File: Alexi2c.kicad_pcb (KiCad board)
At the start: 2 copper layers, 50 x 100 mm, 334 parts, among them J1 Conn_01x04, J10 Conn_01x01, J11 Conn_01x09, J12 Conn_01x02, J13 Conn_01x02, J2 Conn_02x03_Odd_Even, J3 Conn_01x02, J4 Conn_01x10, J5 Conn_01x10, J6 Conn_01x09, J8 Conn_01x01, J9 Conn_01x01, U2 TCA9555PWR, U3 ULN2803A, U4 ULN2803A

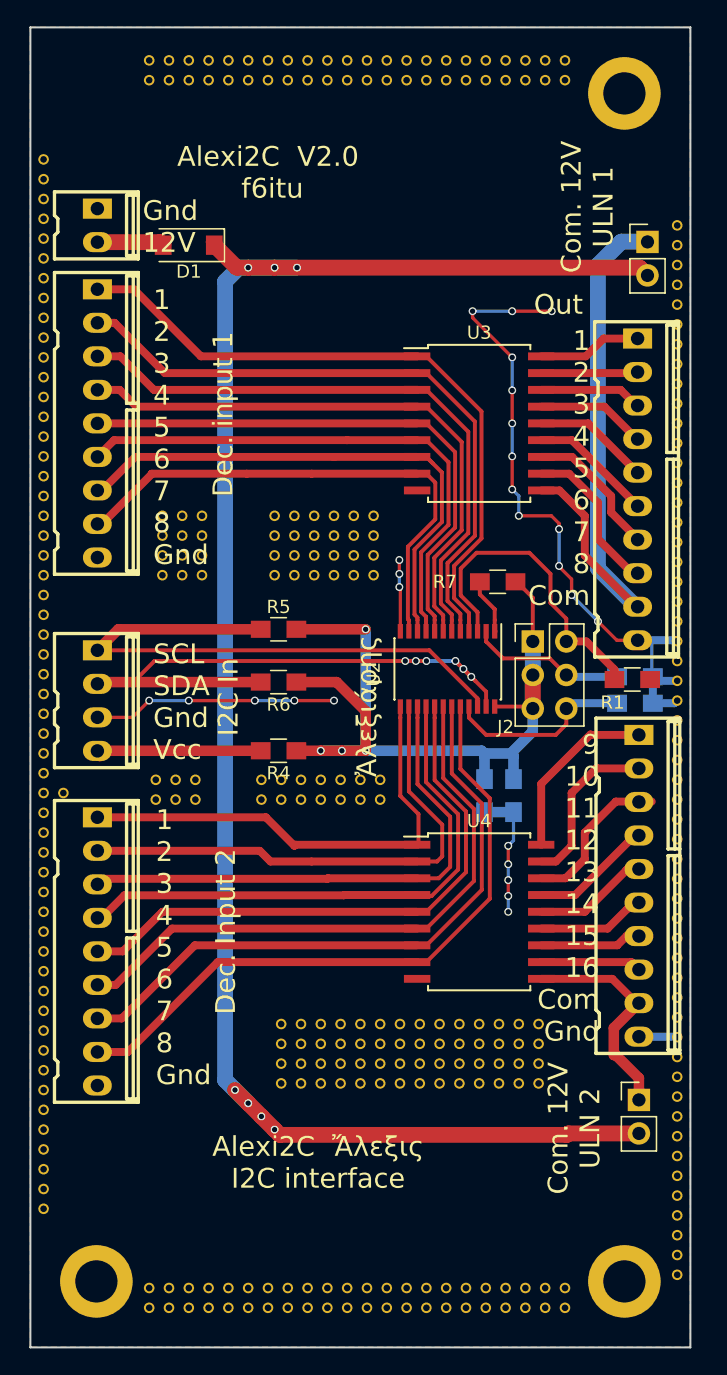
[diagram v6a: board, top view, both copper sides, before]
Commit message: upgrate to Kicad 5.0n, new up to date Gerber
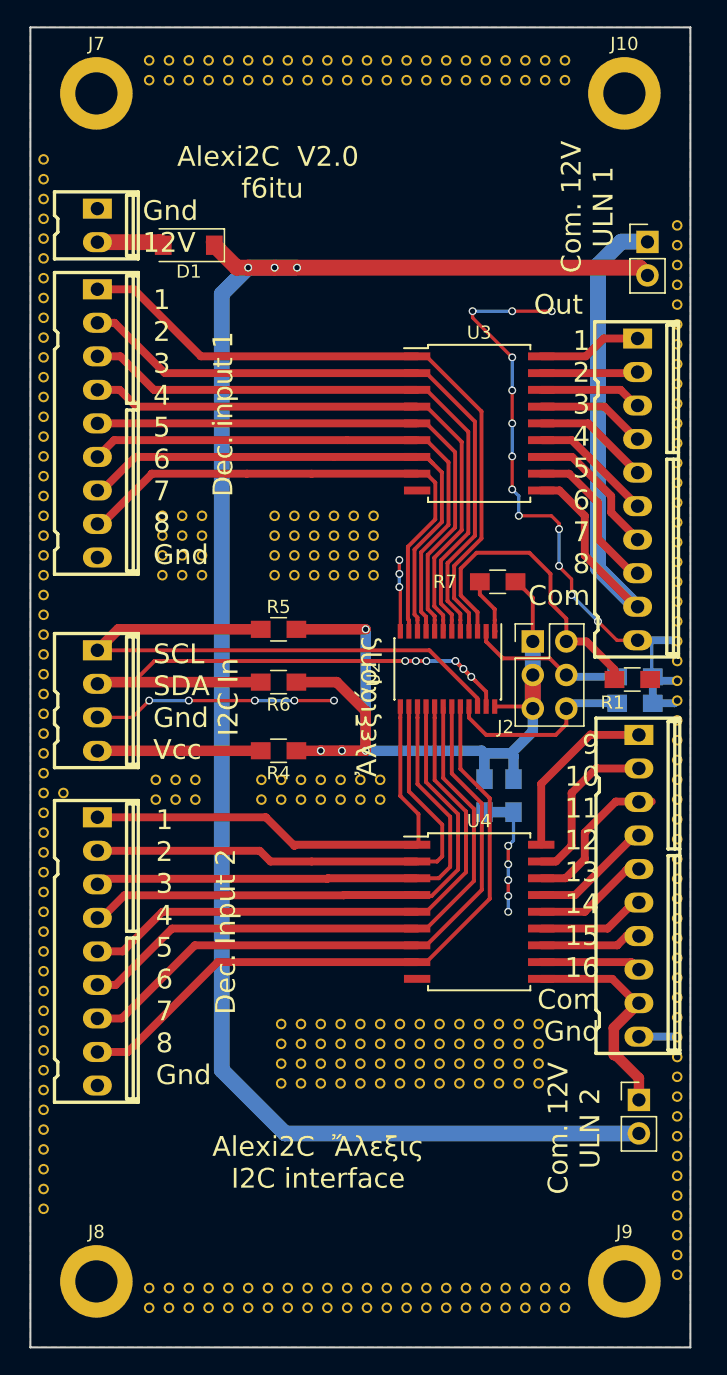
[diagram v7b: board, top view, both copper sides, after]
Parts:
- added J7: Conn_01x01, MountingHole:MountingHole_3.2mm_M3_ISO14580_Pad, F.Cu at (95.0, 40.0)
- J10, J8, J9: footprint Mounting_Holes:MountingHole_3.2mm_M3_ISO14580_Pad -> MountingHole:MountingHole_3.2mm_M3_ISO14580_Pad
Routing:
- net Net-(D1-Pad1): track 138.9 -> 132.7 mm, vias 7 -> 3
